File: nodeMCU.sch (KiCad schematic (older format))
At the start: 38 parts, among them J1 USB_B_Micro, J2 Conn_01x15, J3 Conn_01x15, Q1 S8050, Q2 S8050, SW1 RESET, SW2 FLASH, U1 AP1117-33, U2 CP2102N-A01-GQFN28, U3 ESP-12E

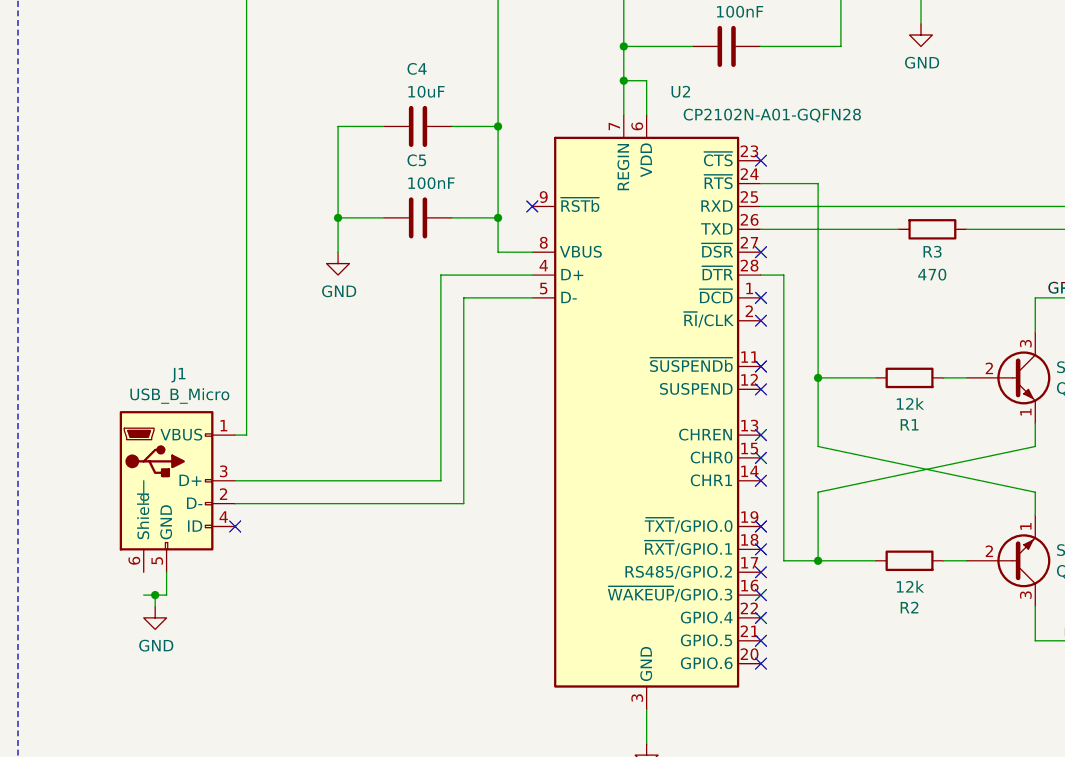
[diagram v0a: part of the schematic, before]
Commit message: Termino el ruteo
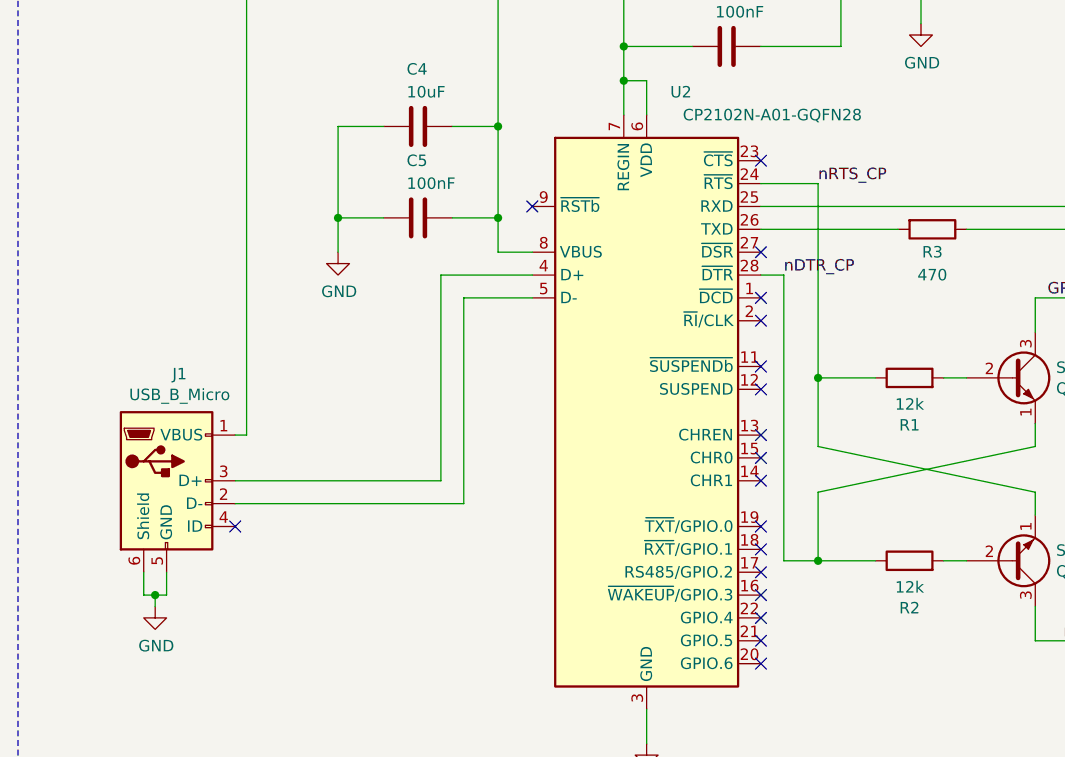
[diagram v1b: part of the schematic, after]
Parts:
- Q2: footprint Package_TO_SOT_SMD:SOT-23 -> Package_TO_SOT_SMD:SOT-23W
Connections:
- net GND: now also J1.6 (Shield)
- net nRTS_CP: now reaches Q2.1 (E), R1.1, U2.24 (~RTS)
- net nDTR_CP: now reaches Q1.1 (E), R2.1, U2.28 (~DTR)
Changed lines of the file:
@@
 F 0 "Q2" H 5141 4446 50  0000 L CNN
 F 1 "S8050" H 5141 4355 50  0000 L CNN
-F 2 "Package_TO_SOT_SMD:SOT-23" H 5150 4325 50  0001 L CIN
+F 2 "Package_TO_SOT_SMD:SOT-23W" H 5150 4325 50  0001 L CIN
 F 3 "http://www.unisonic.com.tw/datasheet/S8050.pdf" H 4950 4400 50  0001 L CNN
 	1    4950 4400
@@
 Wire Wire Line
 	1150 4550 1200 4550
-Wire Wire Line
-	1150 4050 1150 4150
 $Comp
 L power:GND #PWR03
@@
 Wire Wire Line
 	4100 3600 4350 3600
-$Comp
-L Connector:USB_B_Micro J1
-U 1 1 5D04B9AE
-P 1250 4050
-F 0 "J1" H 1307 4517 50  0000 C CNN
-F 1 "USB_B_Micro" H 1307 4426 50  0000 C CNN
-F 2 "Connector_USB:USB_Micro-B_Amphenol_10103594-0001LF_Horizontal" H 1400 4000 50  0001 C CNN
-F 3 "~" H 1400 4000 50  0001 C CNN
-	1    1250 4050
-	1    0    0    -1
-$EndComp
 Wire Wire Line
 	7900 2100 8350 2100
@@
 Wire Wire Line
 	1600 1400 1600 3850
+Wire Wire Line
+	1150 4550 1150 4450
+$Comp
+L Connector:USB_B_Micro J1
+U 1 1 5D04B9AE
+P 1250 4050
+F 0 "J1" H 1307 4517 50  0000 C CNN
+F 1 "USB_B_Micro" H 1307 4426 50  0000 C CNN
+F 2 "Connector_USB:USB_Micro-B_Amphenol_10103594-0001LF_Horizontal" H 1400 4000 50  0001 C CNN
+F 3 "~" H 1400 4000 50  0001 C CNN
+	1    1250 4050
+	1    0    0    -1
+$EndComp
+Text Label 4100 2750 0    50   ~ 0
+nRTS_CP
+Text Label 3950 3150 0    50   ~ 0
+nDTR_CP
 $EndSCHEMATC

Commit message: Agregp logos
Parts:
- removed Q1: S8050, Package_TO_SOT_SMD:SOT-23, symbol Transistor_BJT:S8050
- removed Q2: S8050, Package_TO_SOT_SMD:SOT-23W, symbol Transistor_BJT:S8050
- added Q1, Q2: S8050, Package_TO_SOT_SMD:SOT-23, symbol Device:Q_NPN_BEC
- J1: footprint Connector_USB:USB_Micro-B_Amphenol_10103594-0001LF_Horizontal -> Connector_USB:USB_Micro-B_Molex-105017-0001
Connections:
- net GPIO_0: now also Q1.3 (C)
- net nDTR_CP: now also Q1.2 (E)
- net nRST: now also Q2.3 (C)
- net nRTS_CP: now also Q2.2 (E)
- net at R2.2: now also Q2.1 (B)
- net at R1.2: now also Q1.1 (B)
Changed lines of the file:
@@
 Rev "1.2"
 Comp "Ing. Suarez Sebastian Alejandro"
-Comment1 "https://github.com/nodemcu/nodemcu-devkit-v1.0/blob/master/LICENSE"
-Comment2 "Bajo Licencia MIT"
-Comment3 "Basado en NodeMCU devkit-v1.0 (https://github.com/nodemcu/nodemcu-devkit-v1.0)"
-Comment4 ""
+Comment1 ""
+Comment2 "https://github.com/nodemcu/nodemcu-devkit-v1.0/blob/master/LICENSE"
+Comment3 "Bajo Licencia MIT"
+Comment4 "Basado en NodeMCU devkit-v1.0 (https://github.com/nodemcu/nodemcu-devkit-v1.0)"
 $EndDescr
-$Comp
-L Transistor_BJT:S8050 Q2
-U 1 1 5D014577
-P 4950 4400
-F 0 "Q2" H 5141 4446 50  0000 L CNN
-F 1 "S8050" H 5141 4355 50  0000 L CNN
-F 2 "Package_TO_SOT_SMD:SOT-23W" H 5150 4325 50  0001 L CIN
-F 3 "http://www.unisonic.com.tw/datasheet/S8050.pdf" H 4950 4400 50  0001 L CNN
-	1    4950 4400
-	1    0    0    1
-$EndComp
-$Comp
-L Transistor_BJT:S8050 Q1
-U 1 1 5D0158DF
-P 4950 3600
-F 0 "Q1" H 5141 3554 50  0000 L CNN
-F 1 "S8050" H 5141 3645 50  0000 L CNN
-F 2 "Package_TO_SOT_SMD:SOT-23" H 5150 3525 50  0001 L CIN
-F 3 "http://www.unisonic.com.tw/datasheet/S8050.pdf" H 4950 3600 50  0001 L CNN
-	1    4950 3600
-	1    0    0    -1
-$EndComp
 $Comp
 L Device:R R2
@@
 F 0 "J1" H 1307 4517 50  0000 C CNN
 F 1 "USB_B_Micro" H 1307 4426 50  0000 C CNN
-F 2 "Connector_USB:USB_Micro-B_Amphenol_10103594-0001LF_Horizontal" H 1400 4000 50  0001 C CNN
+F 2 "Connector_USB:USB_Micro-B_Molex-105017-0001" H 1400 4000 50  0001 C CNN
 F 3 "~" H 1400 4000 50  0001 C CNN
 	1    1250 4050
@@
 Text Label 3950 3150 0    50   ~ 0
 nDTR_CP
+$Comp
+L Device:Q_NPN_BEC Q1
+U 1 1 5D1876D5
+P 4950 3600
+F 0 "Q1" H 5140 3646 50  0000 L CNN
+F 1 "S8050" H 5140 3555 50  0000 L CNN
+F 2 "Package_TO_SOT_SMD:SOT-23" H 5150 3700 50  0001 C CNN
+F 3 "~" H 4950 3600 50  0001 C CNN
+	1    4950 3600
+	1    0    0    -1
+$EndComp
+$Comp
+L Device:Q_NPN_BEC Q2
+U 1 1 5D189887
+P 4950 4400
+F 0 "Q2" H 5140 4354 50  0000 L CNN
+F 1 "S8050" H 5140 4445 50  0000 L CNN
+F 2 "Package_TO_SOT_SMD:SOT-23" H 5150 4500 50  0001 C CNN
+F 3 "~" H 4950 4400 50  0001 C CNN
+	1    4950 4400
+	1    0    0    1
+$EndComp
+$Comp
+L Graphic:Logo_Open_Hardware_Small #LOGO?
+U 1 1 5D102E43
+P 10950 6900
+F 0 "#LOGO?" H 10950 7175 50  0001 C CNN
+F 1 "Logo_Open_Hardware_Small" H 10950 6675 50  0001 C CNN
+F 2 "" H 10950 6900 50  0001 C CNN
+F 3 "~" H 10950 6900 50  0001 C CNN
+	1    10950 6900
+	1    0    0    -1
+$EndComp
 $EndSCHEMATC

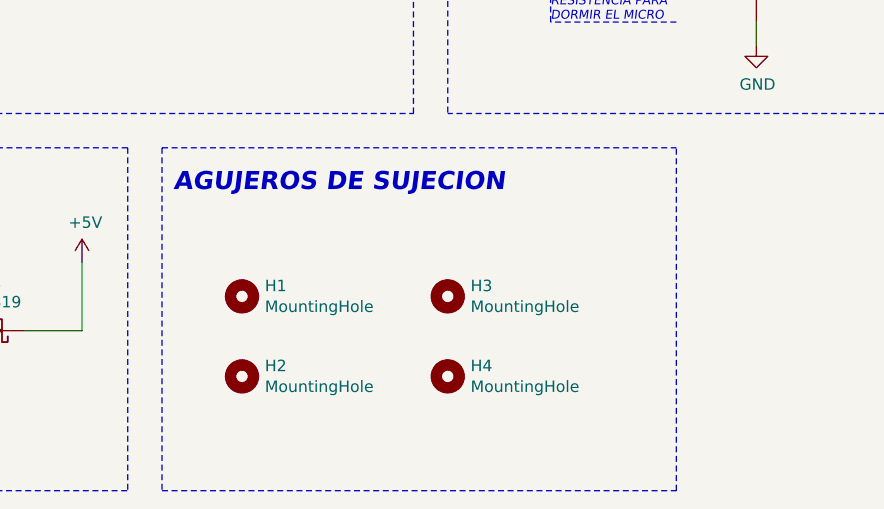
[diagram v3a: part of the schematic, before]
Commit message: Agrego fiducial
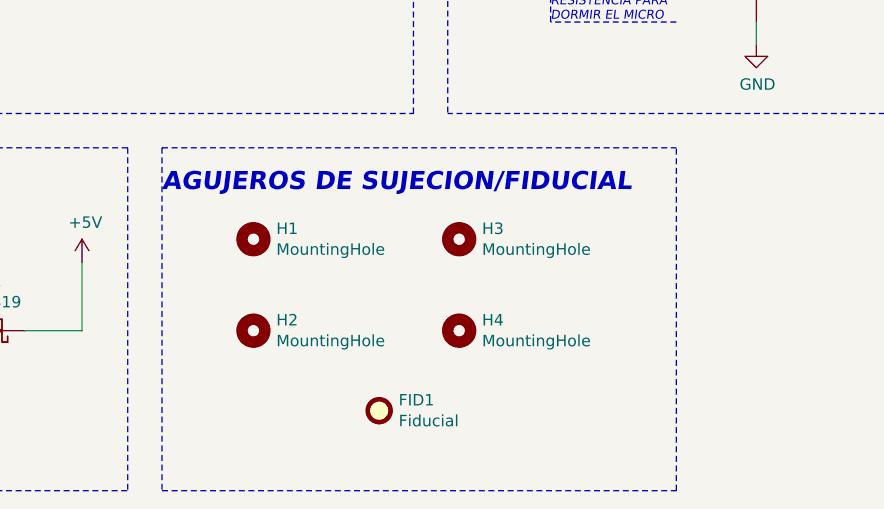
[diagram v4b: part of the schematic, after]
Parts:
- added FID1: Fiducial, Fiducial:Fiducial_1mm_Mask2mm, symbol Mechanical:Fiducial
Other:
- note added: "AGUJEROS DE SUJECION/FIDUCIAL"
- note removed: "AGUJEROS DE SUJECION"
- moved on the sheet: H1, H2, H3, H4
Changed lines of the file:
@@
 L Mechanical:MountingHole H1
 U 1 1 5D1E5AB6
-P 4950 6850
-F 0 "H1" H 5050 6896 50  0000 L CNN
-F 1 "MountingHole" H 5050 6805 50  0000 L CNN
-F 2 "MountingHole:MountingHole_2.2mm_M2" H 4950 6850 50  0001 C CNN
-F 3 "~" H 4950 6850 50  0001 C CNN
-	1    4950 6850
+P 5000 6600
+F 0 "H1" H 5100 6646 50  0000 L CNN
+F 1 "MountingHole" H 5100 6555 50  0000 L CNN
+F 2 "MountingHole:MountingHole_2.2mm_M2" H 5000 6600 50  0001 C CNN
+F 3 "~" H 5000 6600 50  0001 C CNN
+	1    5000 6600
 	1    0    0    -1
 $EndComp
@@
 L Mechanical:MountingHole H3
 U 1 1 5D1E5FD2
-P 5850 6850
-F 0 "H3" H 5950 6896 50  0000 L CNN
-F 1 "MountingHole" H 5950 6805 50  0000 L CNN
-F 2 "MountingHole:MountingHole_2.2mm_M2" H 5850 6850 50  0001 C CNN
-F 3 "~" H 5850 6850 50  0001 C CNN
-	1    5850 6850
+P 5900 6600
+F 0 "H3" H 6000 6646 50  0000 L CNN
+F 1 "MountingHole" H 6000 6555 50  0000 L CNN
+F 2 "MountingHole:MountingHole_2.2mm_M2" H 5900 6600 50  0001 C CNN
+F 3 "~" H 5900 6600 50  0001 C CNN
+	1    5900 6600
 	1    0    0    -1
 $EndComp
@@
 L Mechanical:MountingHole H2
 U 1 1 5D1E64ED
-P 4950 7200
-F 0 "H2" H 5050 7246 50  0000 L CNN
-F 1 "MountingHole" H 5050 7155 50  0000 L CNN
-F 2 "MountingHole:MountingHole_2.2mm_M2" H 4950 7200 50  0001 C CNN
-F 3 "~" H 4950 7200 50  0001 C CNN
-	1    4950 7200
+P 5000 7000
+F 0 "H2" H 5100 7046 50  0000 L CNN
+F 1 "MountingHole" H 5100 6955 50  0000 L CNN
+F 2 "MountingHole:MountingHole_2.2mm_M2" H 5000 7000 50  0001 C CNN
+F 3 "~" H 5000 7000 50  0001 C CNN
+	1    5000 7000
 	1    0    0    -1
 $EndComp
@@
 L Mechanical:MountingHole H4
 U 1 1 5D1E67FE
-P 5850 7200
-F 0 "H4" H 5950 7246 50  0000 L CNN
-F 1 "MountingHole" H 5950 7155 50  0000 L CNN
-F 2 "MountingHole:MountingHole_2.2mm_M2" H 5850 7200 50  0001 C CNN
-F 3 "~" H 5850 7200 50  0001 C CNN
-	1    5850 7200
+P 5900 7000
+F 0 "H4" H 6000 7046 50  0000 L CNN
+F 1 "MountingHole" H 6000 6955 50  0000 L CNN
+F 2 "MountingHole:MountingHole_2.2mm_M2" H 5900 7000 50  0001 C CNN
+F 3 "~" H 5900 7000 50  0001 C CNN
+	1    5900 7000
 	1    0    0    -1
 $EndComp
@@
 Wire Notes Line
 	6850 7700 6850 6200
-Text Notes 4650 6400 0    79   Italic 16
-AGUJEROS DE SUJECION
+Text Notes 4600 6400 0    79   Italic 16
+AGUJEROS DE SUJECION/FIDUCIAL
 Wire Wire Line
 	3850 2750 4100 2750
@@
 $EndComp
 $Comp
-L Graphic:Logo_Open_Hardware_Small #LOGO?
+L Graphic:Logo_Open_Hardware_Small #LOGO1
 U 1 1 5D102E43
 P 10950 6900
-F 0 "#LOGO?" H 10950 7175 50  0001 C CNN
+F 0 "#LOGO1" H 10950 7175 50  0001 C CNN
 F 1 "Logo_Open_Hardware_Small" H 10950 6675 50  0001 C CNN
 F 2 "" H 10950 6900 50  0001 C CNN
@@
 	1    0    0    -1
 $EndComp
+$Comp
+L Mechanical:Fiducial FID1
+U 1 1 5D1470F6
+P 5550 7350
+F 0 "FID1" H 5635 7396 50  0000 L CNN
+F 1 "Fiducial" H 5635 7305 50  0000 L CNN
+F 2 "Fiducial:Fiducial_1mm_Mask2mm" H 5550 7350 50  0001 C CNN
+F 3 "~" H 5550 7350 50  0001 C CNN
+	1    5550 7350
+	1    0    0    -1
+$EndComp

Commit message: Agrego numero de partes
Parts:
- D1: Numero de parte de digikey (none) -> 1N5819HW-FDITR-ND
- U1: Numero de parte de digikey (none) -> AP1117E25G-13-ND
- U2: Numero de parte de digikey (none) -> 336-4826-2-ND
- U3: Numero de parte de digikey (none) -> 1528-2850-ND
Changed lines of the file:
@@
 F 2 "Package_TO_SOT_SMD:SOT-223-3_TabPin2" H 2250 7100 50  0001 C CNN
 F 3 "http://www.diodes.com/datasheets/AP1117.pdf" H 2350 6650 50  0001 C CNN
+F 4 "AP1117E25G-13-ND" H 2250 6900 50  0001 C CNN "Numero de parte de digikey"
 	1    2250 6900
 	1    0    0    -1
@@
 F 2 "Diode_SMD:D_SOD-323_HandSoldering" H 3850 6825 50  0001 C CNN
 F 3 "http://www.vishay.com/docs/88525/1n5817.pdf" H 3850 7000 50  0001 C CNN
+F 4 "1N5819HW-FDITR-ND" H 3850 7000 50  0001 C CNN "Numero de parte de digikey"
 	1    3850 7000
 	-1   0    0    1
@@
 F 1 "CP2102N-A01-GQFN28" H 3900 5050 50  0000 C CNN
 F 2 "Package_DFN_QFN:QFN-28-1EP_5x5mm_P0.5mm_EP3.35x3.35mm" H 3800 2550 50  0001 L CNN
-F 3 "https://www.silabs.com/documents/public/data-sheets/cp2102n-datasheet.pdf" H 3400 3000 50  0001 C CNN
+F 3 "https://www.silabs.com/documents/public/data-sheets/CP2102-9.pdf" H 3400 3000 50  0001 C CNN
+F 4 "336-4826-2-ND" H 3350 3750 50  0001 C CNN "Numero de parte de digikey"
 	1    3350 3750
 	1    0    0    -1
@@
 F 1 "ESP-12E" H 9300 3100 50  0000 C CNN
 F 2 "RF_Module:ESP-12E" H 8950 2300 50  0001 C CNN
-F 3 "http://wiki.ai-thinker.com/_media/esp8266/esp8266_series_modules_user_manual_v1.1.pdf" H 8600 2400 50  0001 C CNN
+F 3 "https://www.elecrow.com/download/ESP-12F.pdf" H 8600 2400 50  0001 C CNN
+F 4 "1528-2850-ND" H 8950 2300 50  0001 C CNN "Numero de parte de digikey"
 	1    8950 2300
 	1    0    0    -1

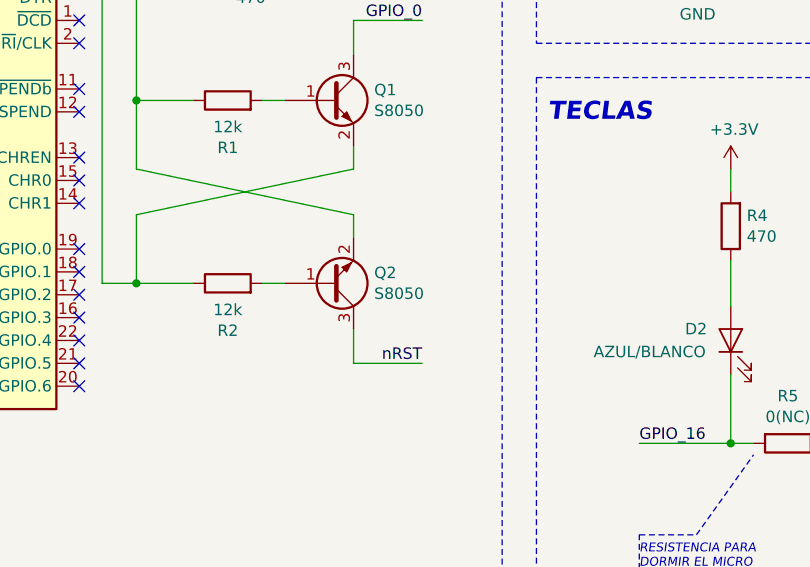
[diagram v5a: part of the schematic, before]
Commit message: Agrego numeros de parte y numero de digikey
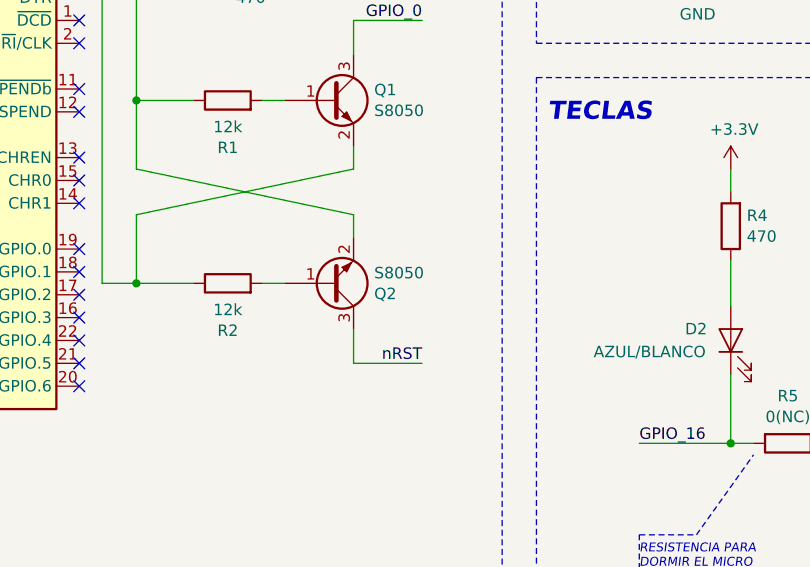
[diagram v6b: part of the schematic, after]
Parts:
- C1, C4, C6: Numero de parte de digikey (none) -> 490-10693-2-ND; Numero de parte del fabricante (none) -> GRM155R60G106ME44D
- C2: Numbero de parte del fabricante (none) -> CL05F104ZO5NNNC; Numero de parte de digikey (none) -> 1276-1004-6-ND
- C3: Numero de parte de digikey (none) -> 478-5257-2-ND; Numero de parte del fabricante (none) -> TAJB106K025RNJ
- C5: Numero de parte del fabricante (none) -> CL05F104ZO5NNNC
- C7: Numero de parte de digikey (none) -> 1276-1004-6-ND; Numero de parte del fabricante (none) -> CL05F104ZO5NNNC
- C8: Numbero de parte de digikey (none) -> 1276-1004-6-ND; Numero de parte del fabricante (none) -> CL05F104ZO5NNNC
- D1: Numero de parte del fabricante (none) -> 1N5819HW-7-F
- D2: Numero de parte de digikey (none) -> 1516-1057-2-ND; Numero de parte del fabricante (none) -> QBLP601-IW
- J1: Numero de parte de digikey (none) -> 609-4618-6-ND; Numero de parte del fabricante (none) -> 10118194-0001LF
- J2: Numero de parte de digikey (none) -> A24931-ND; Numero de parte del fabricante (none) -> 1-640452-5
- J3: Numero de parte de digikey  (none) -> A24931-ND; Numero de parte del fabricante (none) -> 1-640452-5
- Q1, Q2: Numero de parte de digikey (none) -> MMSS8050-H-TPMSTR-ND; Numero de parte del fabricante (none) -> MMSS8050-H-TP
- R1, R10, R11, R12, R2, R8, R9: Numero de parte de di (none) -> YAG6226TR-ND; Numero de parte del fabricante (none) -> RC0100FR-0712KL
- R13: Numero de parte de digikey (none) -> A129655TR-ND; Numero de parte del fabricante (none) -> CRGCQ0402F220K
- R14: Numero de parte de digikey (none) -> MCS0402-100K-CFCT-ND; Numero de parte del fabricante (none) -> MCS04020C1003FE000
- R3: Numero de parte de digikey (none) -> P470DCTR-ND; Numero de partedel fabricante (none) -> ERA-2AEB471X
- R4, R6, R7: Numero de parte de digikey (none) -> P470DCTR-ND; Numero de parte del fabricante (none) -> ERA-2AEB471X
- U1: Numero de parte del fabricante (none) -> AP1117E25G-13
- U2: Numero de parte del fabricante (none) -> CP2102N-A01-GQFN20R
- U3: Numero de parte del fabricante (none) -> 4065

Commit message: Correcciones propuestas II
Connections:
- net nDTR_CP: no longer names the net of Q1.2 (E), R2.1, U2.28 (~DTR)
- net nRTS_CP: no longer names the net of Q2.2 (E), R1.1, U2.24 (~RTS)
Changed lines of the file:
@@
 Sheet 1 1
 Title "NodeMCU"
-Date "2019-06-23"
-Rev "1.2"
-Comp "Ing. Suarez Sebastian Alejandro"
+Date "2019-06-30"
+Rev "1.3"
+Comp "Ing. Suarez Sebastian Alejandro - Revisor: Ferreyra Hernan"
 Comment1 ""
 Comment2 "https://github.com/nodemcu/nodemcu-devkit-v1.0/blob/master/LICENSE"
@@
 AGUJEROS DE SUJECION/FIDUCIAL
 Wire Wire Line
-	3850 2750 4100 2750
-Wire Wire Line
 	4100 4100 4100 4400
 Wire Wire Line
@@
 	3950 4400 4100 4400
 Connection ~ 4100 4400
-Wire Wire Line
-	4100 3600 4100 2750
-Connection ~ 4100 3600
 Wire Wire Line
 	3850 2850 5350 2850
@@
 	1    0    0    -1
 $EndComp
-Text Label 4100 2750 0    50   ~ 0
-nRTS_CP
-Text Label 3950 3150 0    50   ~ 0
-nDTR_CP
 $Comp
 L Device:Q_NPN_BEC Q1
@@
 	1    0    0    1
 $EndComp
+Connection ~ 4100 3600
+Wire Wire Line
+	4100 3600 4100 2750
+Wire Wire Line
+	3850 2750 4100 2750
 $EndSCHEMATC
